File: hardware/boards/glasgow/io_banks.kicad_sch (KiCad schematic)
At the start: 27 parts, among them J10 AUX, J4 Conn_01x02, J5 PinHeader_2x22_P1.27mm, U30 ICE40HX8K-BG121, U32 SN74LVC1T45DCKR

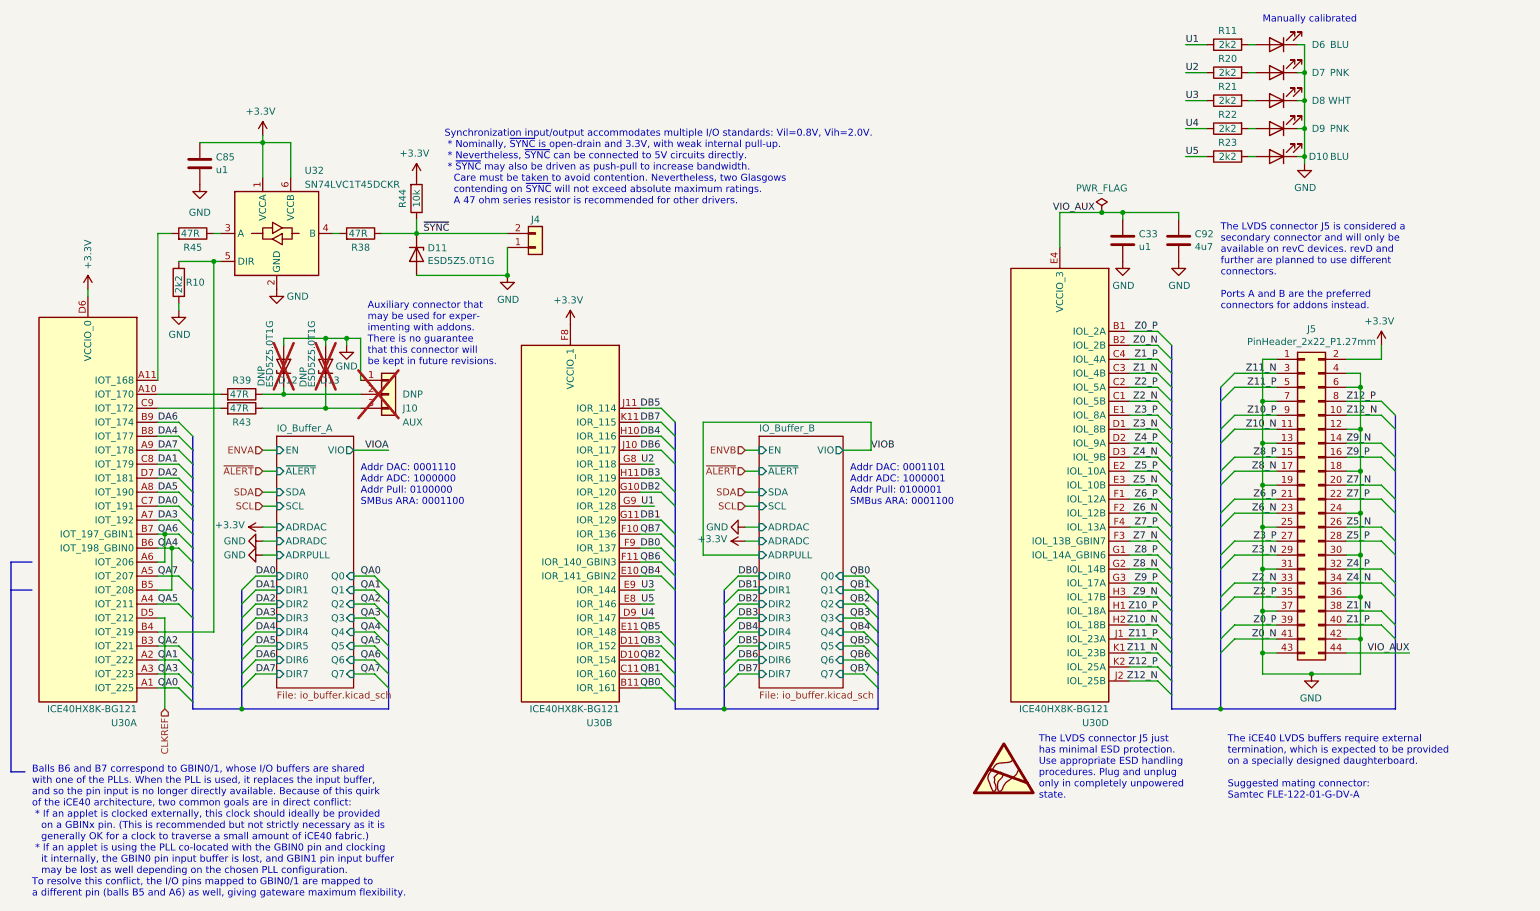
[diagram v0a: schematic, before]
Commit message: JLCPCB part swaps
Switch parts to be either of:
- cheaper
- in stock
- order-able
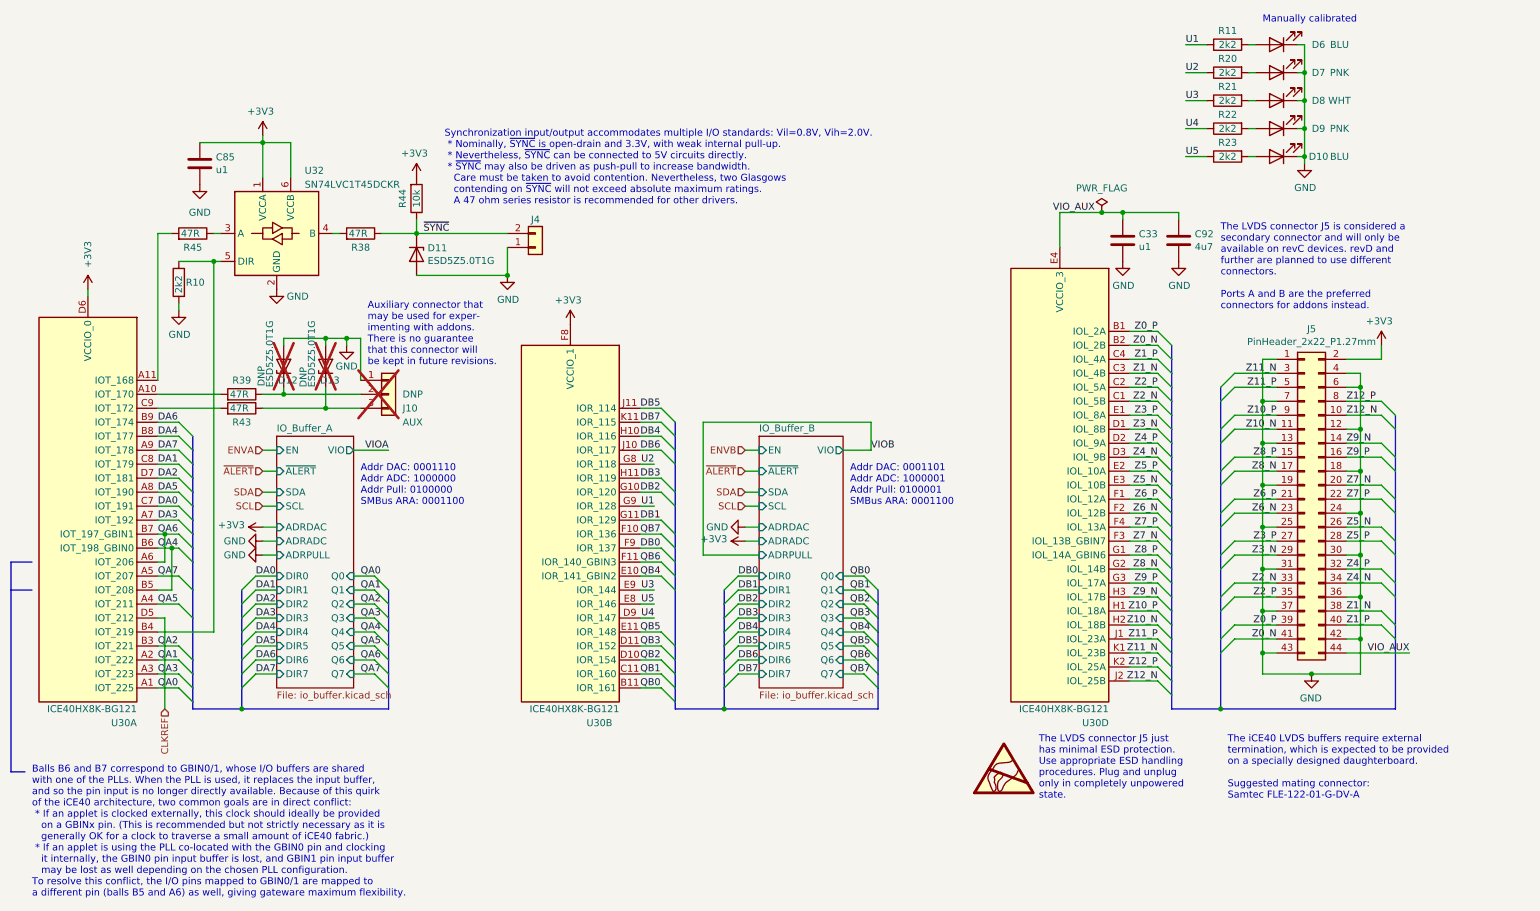
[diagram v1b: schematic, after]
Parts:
- J10: now left out of the parts list
